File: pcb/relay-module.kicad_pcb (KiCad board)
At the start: 4 copper layers, 50 x 50 mm, 59 parts, among them J1 AVR-UPDI-6, J2 QWICC, J3 Power In, J4 Power Out, K1 PR24-5V-900-1A, P1 MountingHole_Pad, P2 MountingHole_Pad, P3 MountingHole_Pad, P4 MountingHole_Pad, Q1 MMBT3904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

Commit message: Changed 5v to orange LED
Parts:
- D3: value Blue -> Orange
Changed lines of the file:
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@@
 				(font
 					(size 0.001 0.001)
+					(thickness 0.15)
 				)
 			)
@@
 				(font
 					(size 0.001 0.001)
+					(thickness 0.15)
 				)
 			)
@@
 				(font
 					(size 0.001 0.001)
+					(thickness 0.15)
 				)
 			)
@@
 				(font
 					(size 0.001 0.001)
+					(thickness 0.15)
 				)
 			)
@@
 				(font
 					(size 0.001 0.001)
+					(thickness 0.15)
 				)
 			)
@@
 				(font
 					(size 0.001 0.001)
+					(thickness 0.15)
 				)
 			)
@@
 				(font
 					(size 0.001 0.001)
+					(thickness 0.15)
 				)
 			)
@@
 				(font
 					(size 0.001 0.001)
+					(thickness 0.15)
 				)
 			)
@@
 				(font
 					(size 0.001 0.001)
+					(thickness 0.15)
 				)
 			)
@@
 				(font
 					(size 0.001 0.001)
+					(thickness 0.15)
 				)
 			)
@@
 				(font
 					(size 0.001 0.001)
+					(thickness 0.15)
 				)
 			)
@@
 				(font
 					(size 0.001 0.001)
+					(thickness 0.15)
 				)
 			)
@@
 				(font
 					(size 0.001 0.001)
+					(thickness 0.15)
 				)
 			)
@@
 				(font
 					(size 0.001 0.001)
+					(thickness 0.15)
 				)
 			)
@@
 				(font
 					(size 0.001 0.001)
+					(thickness 0.15)
 				)
 			)
@@
 				(font
 					(size 0.001 0.001)
+					(thickness 0.15)
 				)
 			)
@@
 			)
 		)
-		(property "Value" "Blue"
+		(property "Value" "Orange"
 			(at 0 1.43 0)
 			(layer "F.Fab")
@@
 			)
 		)
-		(property "Description" "20mA 240mcd Colorless Blue 120° 70mW 3.3V 0603"
+		(property "Description" "20mA 315mcd Colorless Orange 120° 50mW 2.3V 0603"
 			(at 0 0 0)
 			(layer "F.Fab")
@@
 			)
 		)
-		(property "MPN" "XL-1608UBC-04"
+		(property "MPN" "XL-1608UOC-06"
 			(at 0 0 180)
 			(unlocked yes)
@@
 			)
 		)
-		(property "Mouser" "710-150060BS75020"
+		(property "Mouser" "859-LTST-C190KFKT"
 			(at 0 0 180)
 			(unlocked yes)
@@
 			)
 		)
-		(property "Digikey" "5962-XL-1608UBC-04TR-ND"
+		(property "Digikey" "5962-XL-1608UOC-06TR-ND"
 			(at 0 0 180)
 			(unlocked yes)
@@
 			)
 		)
-		(property "LCSC" "C965807"
+		(property "LCSC" "C965800"
 			(at 0 0 180)
 			(unlocked yes)
@@
 				(font
 					(size 0.001 0.001)
+					(thickness 0.15)
 				)
 			)
@@
 				(font
 					(size 0.001 0.001)
+					(thickness 0.15)
 				)
 			)

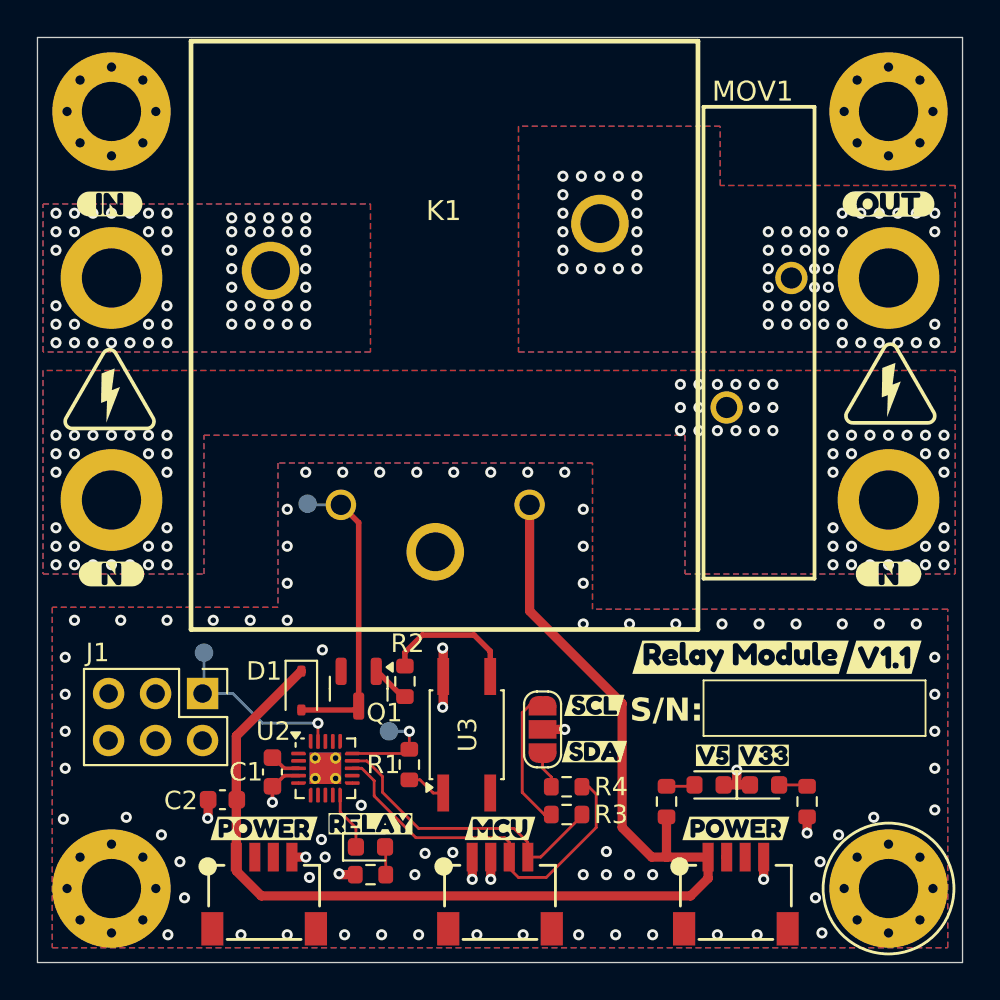
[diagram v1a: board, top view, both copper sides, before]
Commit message: Refined relay based testing
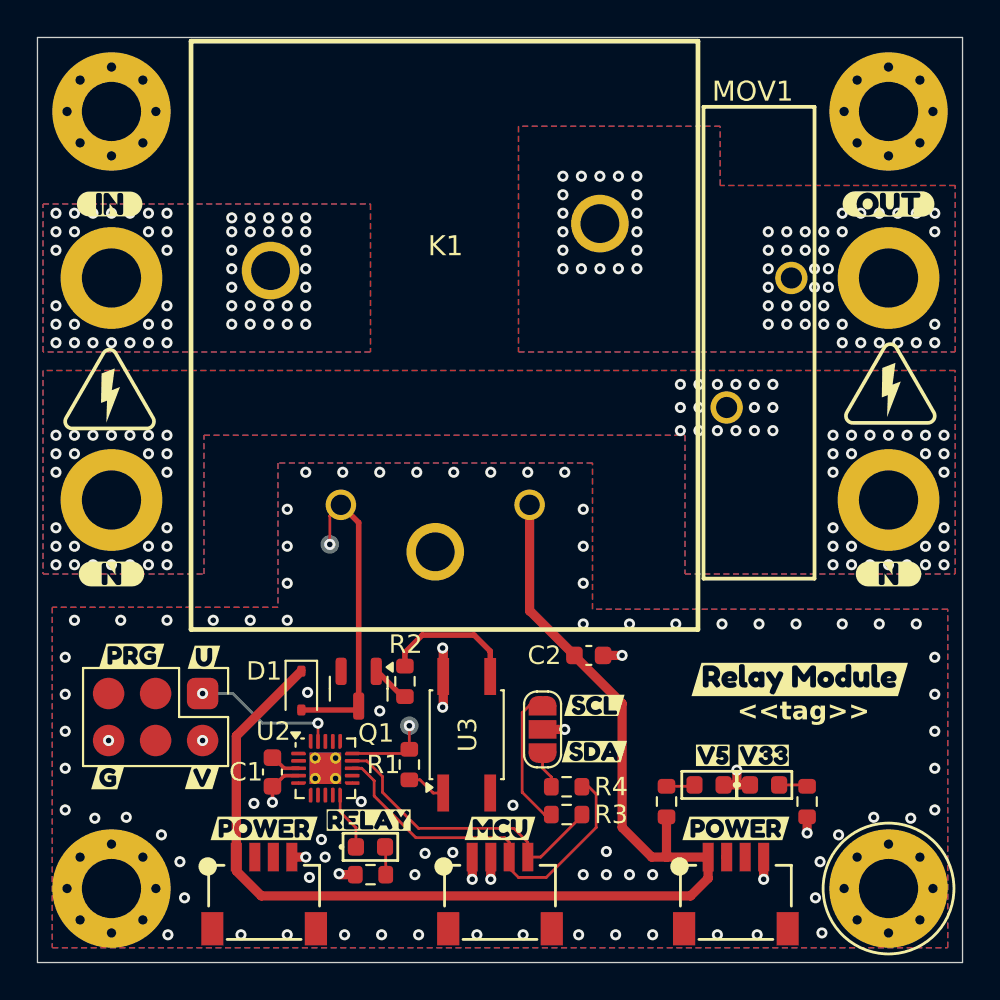
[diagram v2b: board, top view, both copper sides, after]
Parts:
- removed kibuzzard-6802999E: G***, kibuzzard-6802999E
- removed kibuzzard-68227700: G***, kibuzzard-68227700
- added TP4: V33, TestPoint:TestPoint_Pad_D1.0mm, B.Cu at (58.9, 138.0)
- added TP5: GND, TestPoint:TestPoint_Pad_D1.0mm, B.Cu at (53.9, 138.0)
- added kibuzzard-68464303: G***, kibuzzard-68464303, B.Cu at (65.8, 128.8)
- added kibuzzard-68464325: G***, kibuzzard-68464325, B.Cu at (58.9, 134.0)
- added kibuzzard-6846441D: G***, kibuzzard-6846441D, B.Cu at (70.1, 138.7)
- added kibuzzard-684644DA: G***, kibuzzard-684644DA, B.Cu at (58.9, 139.5)
- added kibuzzard-684644E7: G***, kibuzzard-684644E7, B.Cu at (53.9, 136.4)
- added kibuzzard-684647EC: G***, kibuzzard-684647EC, F.Cu at (55.1, 133.4)
- added kibuzzard-68464801: G***, kibuzzard-68464801, F.Cu at (59.0, 133.5)
- added kibuzzard-68464812: G***, kibuzzard-68464812, F.Cu at (53.8, 140.0)
- added kibuzzard-68464817: G***, kibuzzard-68464817, F.Cu at (58.9, 140.0)
- J1: footprint Connector_PinHeader_2.54mm:PinHeader_2x03_P2.54mm_Vertical -> CRGM Connector:PinHeader_2x03_P2.54mm_Vertical_SMD
- LOGO1: footprint CRGM Logos:Aquarius Logo 5mm -> CRGM Logos:Aquarius Logo 10mm
- LOGO3: footprint CRGM Logos:FNWW Face 5mm -> CRGM Logos:FNWW Face 10mm
- TP1: value RELAY_CONTROL -> RELAY_CTRL
- TP2: value RELAY_CTRL -> RELAY_EN
- moved C2 21.3 mm to (79.8, 133.4), turned to 0 degrees
- moved LOGO5 14.2 mm to (82.9, 137.8)
- moved LOGO3 6.36 mm to (75.1, 141.8)
- moved kibuzzard-6822769A 3.42 mm to (91.2, 134.7)
- moved TP1 2.51 mm to (65.8, 127.4)
- moved TP3 2.21 mm to (58.9, 135.5)
- moved LOGO1 2.17 mm to (73.8, 111.4)
- moved TP2 1.14 mm to (70.1, 137.2)
- moved kibuzzard-68029C11 0.50 mm to (75.0, 117.1)
- moved kibuzzard-682275E1 0.22 mm to (67.9, 142.3)
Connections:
- net /RELAY_CONTROL renamed /RELAY_CTRL
- net RELAY_CTRL renamed RELAY_EN
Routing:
- net UPDI: track 10.1 -> 7.99 mm, vias 1 -> 2
- net RELAY_EN: track 4.69 -> 3.89 mm
- net /RELAY_CTRL: track 16.3 -> 16.9 mm, vias 0 -> 1
- net GND: track 6.21 -> 6.22 mm, vias 77 -> 83
- net +3.3V: vias 9 -> 10
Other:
- board text added: "<<hash>>"
- board text added: "<<tag>>"
- board text removed: "S/N:"

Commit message: Fixed missing LCSC part numbers; updated CI script
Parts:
- J2, J3, J4: footprint CRGM Connector:SM04B-SRSS-TB -> CRGM Connector:JST_SH_SM04B-SRSS-TB_1x04-1MP_P1.00mm_Horizontal
- moved J3 2.00 mm to (87.7, 146.3), turned to 0 degrees
- moved J4 2.00 mm to (62.2, 146.3), turned to 0 degrees
- moved J2 2.00 mm to (75.0, 146.3), turned to 0 degrees

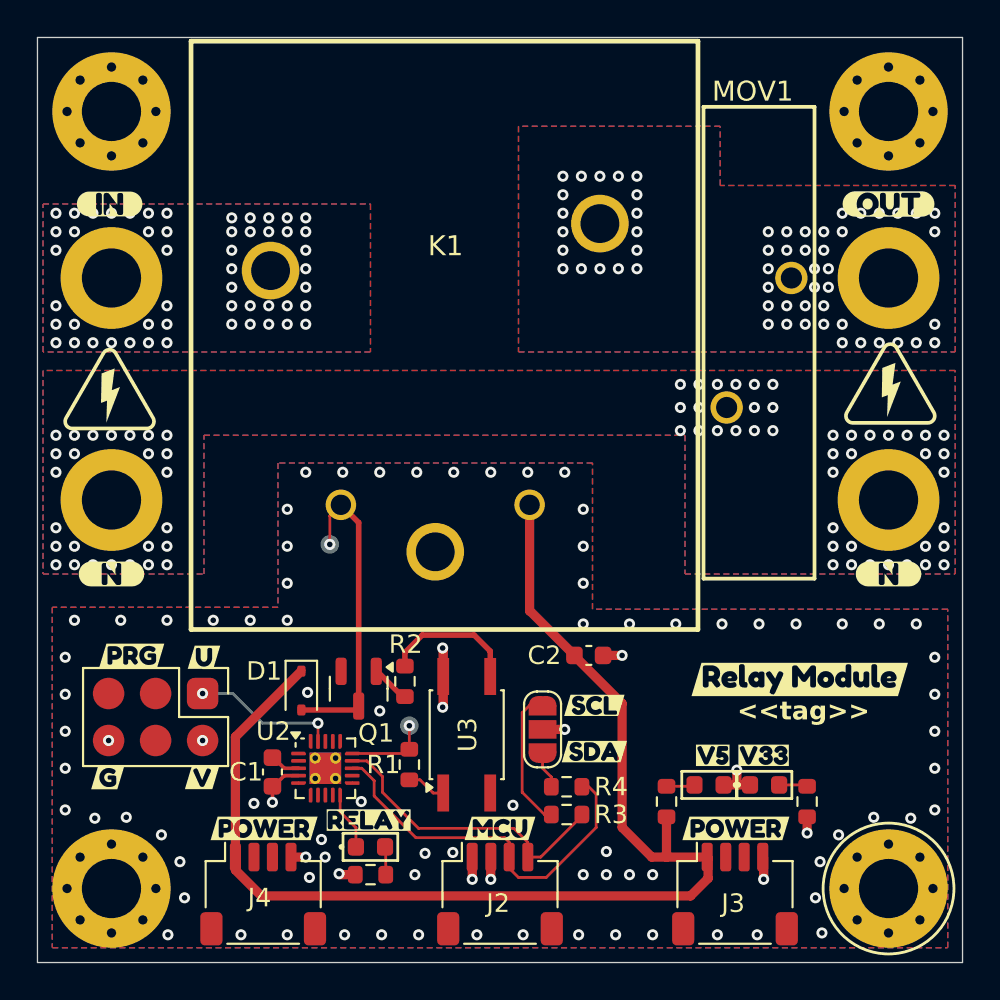
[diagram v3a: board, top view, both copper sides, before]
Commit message: Rerouted after adding test points
Added test points to all pins
Added serial connector
Added relay LED
Changed symbols and footprints to CRGM
Moved pins around to optimize routing
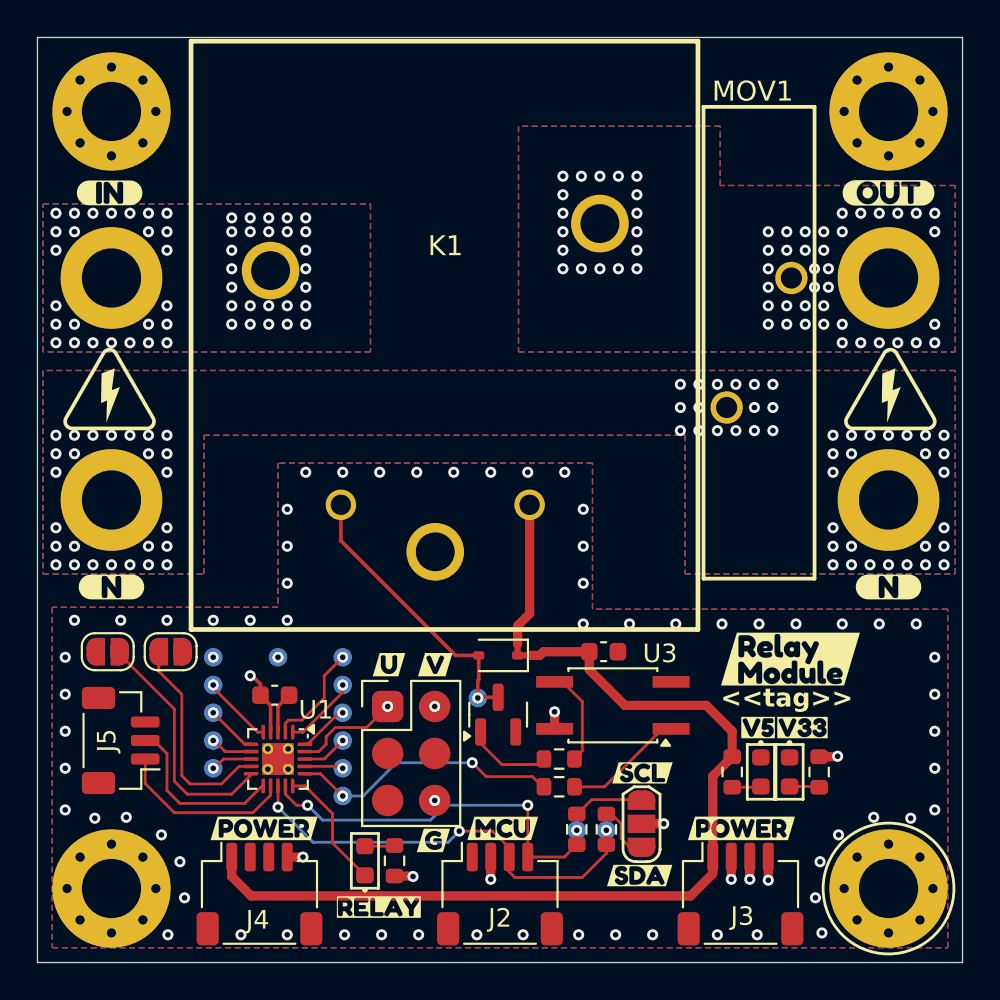
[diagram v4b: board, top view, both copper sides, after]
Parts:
- removed U2: ATtiny1616-M, CRG Makes:VQFN-20-1EP_3x3mm_P0.4mm_EP1.7x1.7mm_ThermalVias
- removed kibuzzard-6822769A: G***, kibuzzard-6822769A
- removed kibuzzard-68464303: G***, kibuzzard-68464303
- removed kibuzzard-68464325: G***, kibuzzard-68464325
- removed kibuzzard-6846441D: G***, kibuzzard-6846441D
- removed kibuzzard-684644DA: G***, kibuzzard-684644DA
- removed kibuzzard-684644E7: G***, kibuzzard-684644E7
- removed kibuzzard-684647EC: G***, kibuzzard-684647EC
- added J5: ~, Connector_JST:JST_SH_BM03B-SRSS-TB_1x03-1MP_P1.00mm_Vertical, F.Cu at (54.5, 138.0)
- added JP2: A0, CRGM Connector:SolderJumper-2_P1.3mm_Open_RoundedPad1.0x1.5mm, F.Cu at (53.8, 133.2)
- added JP3: A1, CRGM Connector:SolderJumper-2_P1.3mm_Open_RoundedPad1.0x1.5mm, F.Cu at (57.2, 133.2)
- added TP10: PA3, CRGM Mechanical:TestPoint_Pad_D1.0mm, B.Cu at (66.5, 133.5)
- added TP11: PA4, CRGM Mechanical:TestPoint_Pad_D1.0mm, B.Cu at (59.5, 135.0)
- added TP12: PA5, CRGM Mechanical:TestPoint_Pad_D1.0mm, B.Cu at (59.5, 136.5)
- added TP13: PA6, CRGM Mechanical:TestPoint_Pad_D1.0mm, B.Cu at (59.5, 138.0)
- added TP14: PA7, CRGM Mechanical:TestPoint_Pad_D1.0mm, B.Cu at (59.5, 139.5)
- added TP15: SCL, CRGM Mechanical:TestPoint_Pad_D1.0mm, B.Cu at (79.2, 142.8)
- added TP16: SDA, CRGM Mechanical:TestPoint_Pad_D1.0mm, B.Cu at (80.8, 142.8)
- added TP6: PC2, CRGM Mechanical:TestPoint_Pad_D1.0mm, B.Cu at (66.5, 139.5)
- added TP7: PC3, CRGM Mechanical:TestPoint_Pad_D1.0mm, B.Cu at (66.5, 138.0)
- added TP8: PA1, CRGM Mechanical:TestPoint_Pad_D1.0mm, B.Cu at (66.5, 136.5)
- added TP9: PA2, CRGM Mechanical:TestPoint_Pad_D1.0mm, B.Cu at (66.5, 135.0)
- added U1: ATtiny1616-MNR, CRG Makes:VQFN-20-1EP_3x3mm_P0.4mm_EP1.7x1.7mm_ThermalVias, F.Cu at (63.0, 139.0)
- added kibuzzard-68226E29: G***, kibuzzard-68226E29, B.Cu at (79.2, 144.3)
- added kibuzzard-68226E38: G***, kibuzzard-68226E38, B.Cu at (80.7, 141.4)
- added kibuzzard-6855E3B5: G***, kibuzzard-6855E3B5, F.Cu at (90.7, 133.6)
- added kibuzzard-6855E9AE: G***, kibuzzard-6855E9AE, B.Cu at (69.0, 134.5)
- added kibuzzard-6855E9B6: G***, kibuzzard-6855E9B6, B.Cu at (73.8, 134.4)
- added kibuzzard-68560765: G***, kibuzzard-68560765, B.Cu at (64.3, 136.5)
- added kibuzzard-6856076F: G***, kibuzzard-6856076F, B.Cu at (64.2, 135.0)
- added kibuzzard-68560785: G***, kibuzzard-68560785, B.Cu at (68.8, 137.9)
- added kibuzzard-68560793: G***, kibuzzard-68560793, B.Cu at (68.8, 139.5)
- added kibuzzard-6856079F: G***, kibuzzard-6856079F, B.Cu at (68.8, 141.0)
- added kibuzzard-685607AD: G***, kibuzzard-685607AD, B.Cu at (68.8, 133.4)
- added kibuzzard-685607D3: G***, kibuzzard-685607D3, B.Cu at (61.4, 133.5)
- added kibuzzard-685607DD: G***, kibuzzard-685607DD, B.Cu at (57.5, 133.5)
- added kibuzzard-685607E7: G***, kibuzzard-685607E7, B.Cu at (57.2, 135.0)
- added kibuzzard-68560824: G***, kibuzzard-68560824, B.Cu at (57.2, 136.5)
- added kibuzzard-68560831: G***, kibuzzard-68560831, B.Cu at (57.2, 138.0)
- added kibuzzard-6856083D: G***, kibuzzard-6856083D, B.Cu at (57.2, 139.5)
- JP1: footprint Jumper:SolderJumper-3_P1.3mm_Open_RoundedPad1.0x1.5mm_NumberLabels -> CRGM Connector:SolderJumper-3_P1.3mm_Open_RoundedPad1.0x1.5mm
- R3, R4: value 10K -> 4.7K
- TP1, TP2, TP3, TP4, TP5: footprint TestPoint:TestPoint_Pad_D1.0mm -> CRGM Mechanical:TestPoint_Pad_D1.0mm
- moved kibuzzard-68464812 17.9 mm to (71.4, 143.4)
- moved kibuzzard-68464817 14.0 mm to (71.5, 133.9)
- moved LOGO3 13.1 mm to (88.2, 141.5)
- moved LOGO5 12.7 mm to (95.4, 135.2)
- moved TP1 11.5 mm to (73.8, 135.7)
- moved D1 10.8 mm to (74.9, 133.4), turned to 180 degrees
- moved TP5 10.2 mm to (63.0, 133.5)
- moved J1 10.0 mm to (68.9, 136.2), turned to 0 degrees
- moved kibuzzard-68464801 10.0 mm to (69.0, 133.9)
- moved TP3 10.00 mm to (68.9, 136.2)
- moved R2 9.34 mm to (78.2, 139.0), turned to 180 degrees
- moved R1 8.19 mm to (78.2, 140.5), turned to 0 degrees
- moved U3 8.06 mm to (81.1, 136.1), turned to 180 degrees
- moved Q1 7.67 mm to (74.9, 136.6), turned to 90 degrees
- moved JP1 7.39 mm to (82.7, 142.5)
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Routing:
- net /A0: track 0.00 -> 13.1 mm
- net /A1: track 0.00 -> 11.5 mm
- net RELAY_EN: track 3.89 -> 14.7 mm, vias 1 -> 2
- net TXD: track 0.00 -> 9.65 mm
- net RXD: track 0.00 -> 9.35 mm
- net +5V: track 66.9 -> 58.6 mm
- net /PA3: track 0.00 -> 5.76 mm, vias 0 -> 1
- net /SCL: track 16.5 -> 21.0 mm, vias 0 -> 3
- net Net-(R1-Pad2): track 2.14 -> 6.52 mm
- net /PA2: track 0.00 -> 3.99 mm, vias 0 -> 1
- net /PA4: track 0.00 -> 3.84 mm, vias 0 -> 1
- net Net-(JP1-A): track 7.64 -> 3.82 mm
- net RELAY_LED: track 3.15 -> 6.81 mm
- net /SDA: track 20.8 -> 23.6 mm, vias 0 -> 3
- net /PA5: track 0.00 -> 2.75 mm, vias 0 -> 1
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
